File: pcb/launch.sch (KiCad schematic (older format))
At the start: 241 parts, among them J1 DNP, U1 ATmega32U4-MU, Y0 ECS-160-18-23G-JGN-TR

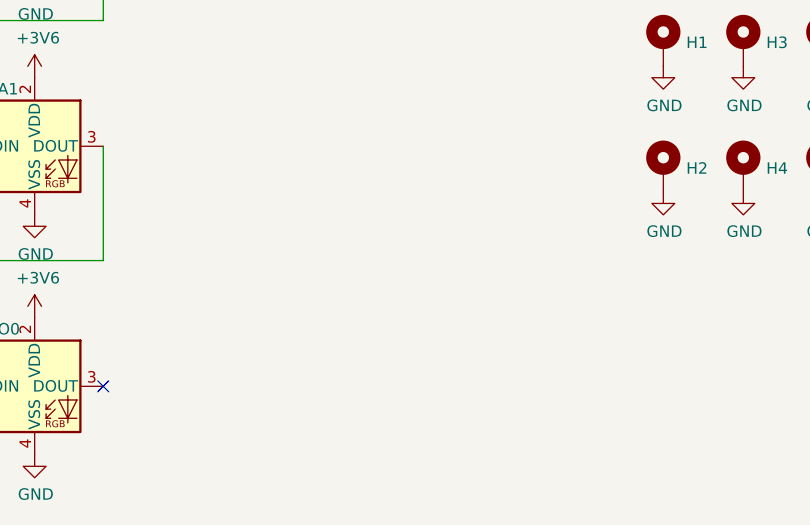
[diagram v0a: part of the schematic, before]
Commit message: add logo to schematic, link with PCB
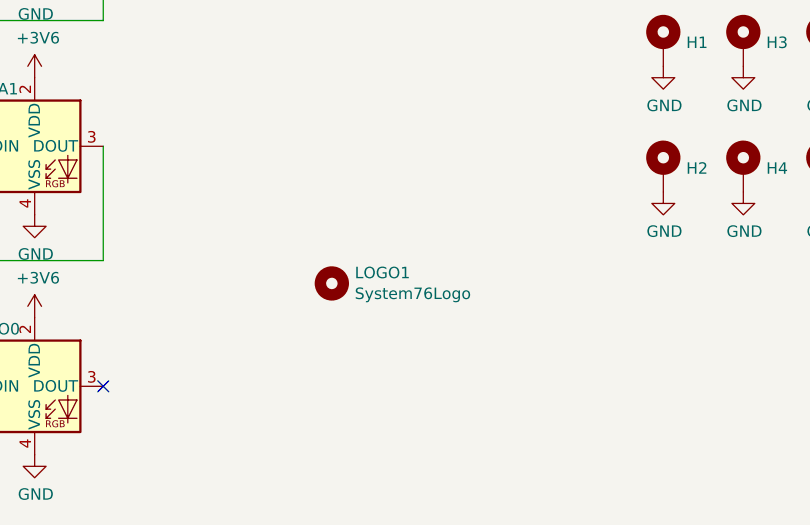
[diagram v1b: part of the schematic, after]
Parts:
- added LOGO1: System76Logo, Logo:System76, symbol Mechanical:MountingHole
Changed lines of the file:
@@
+	1    0    0    -1
+$EndComp
+$Comp
+L Mechanical:MountingHole LOGO1
+U 1 1 60A8F9E7
+P 10700 10100
+F 0 "LOGO1" H 10800 10146 50  0000 L CNN
+F 1 "System76Logo" H 10800 10055 50  0000 L CNN
+F 2 "Logo:System76" H 10700 10100 50  0001 C CNN
+F 3 "~" H 10700 10100 50  0001 C CNN
+	1    10700 10100
 	1    0    0    -1
 $EndComp

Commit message: Fix library references for symbols renamed in upstream also remove cache from gitignore, include in repo in case user's libaries don't align.
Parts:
- D10, D11, D12, D13, D14, D15, D16, D17, D18, D19, D20, D21, D22, D23, D24, D25, D26, D27, D28, D29, D30, D31, D32, D33, D34, D35, D36, D37, D38, D39, D40, D41, D42, D43, D44, D45, D46, D47, D48, D49, D50, D9: symbol Device:D_x2_KCom_AAK -> Device:D_Dual_CommonCathode_AAK
- U1: symbol MCU_Microchip_ATmega:ATmega32U4-MU -> MCU_Microchip_ATmega:ATmega32U4-M
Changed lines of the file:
@@
 LED
 $Comp
-L MCU_Microchip_ATmega:ATmega32U4-MU U1
+L MCU_Microchip_ATmega:ATmega32U4-M U1
 U 1 1 5E72DD65
 P 14600 6200
@@
 Wire Wire Line
 	14500 8000 14600 8000
-Connection ~ 14600 8000
 Text GLabel 15200 4800 2    50   Input ~ 0
 SCLK
@@
 Connection ~ 1750 2300
 $Comp
-L Device:D_x2_KCom_AAK D9
+L Device:D_Dual_CommonCathode_AAK D9
 U 1 1 6068616E
 P 1750 1500
@@
 $EndComp
 $Comp
-L Device:D_x2_KCom_AAK D10
+L Device:D_Dual_CommonCathode_AAK D10
 U 1 1 6097330F
 P 1750 2000
@@
 	2450 1500 2450 2000
 $Comp
-L Device:D_x2_KCom_AAK D11
+L Device:D_Dual_CommonCathode_AAK D11
 U 1 1 60994697
 P 1750 2500
@@
 	950  4300 1750 4300
 $Comp
-L Device:D_x2_KCom_AAK D12
+L Device:D_Dual_CommonCathode_AAK D12
 U 1 1 60A3ED72
 P 1750 3000
@@
 $EndComp
 $Comp
-L Device:D_x2_KCom_AAK D13
+L Device:D_Dual_CommonCathode_AAK D13
 U 1 1 60A3F73E
 P 1750 3500
@@
 $EndComp
 $Comp
-L Device:D_x2_KCom_AAK D14
+L Device:D_Dual_CommonCathode_AAK D14
 U 1 1 60A40011
 P 1750 4000
@@
 Connection ~ 11050 5800
 $Comp
-L Device:D_x2_KCom_AAK D15
+L Device:D_Dual_CommonCathode_AAK D15
 U 1 1 60CB7B22
 P 10750 1500
@@
 $EndComp
 $Comp
-L Device:D_x2_KCom_AAK D16
+L Device:D_Dual_CommonCathode_AAK D16
 U 1 1 60CC23F5
 P 10750 2000
@@
 $EndComp
 $Comp
-L Device:D_x2_KCom_AAK D18
+L Device:D_Dual_CommonCathode_AAK D18
 U 1 1 60CC3D8E
 P 10750 3000
@@
 $EndComp
 $Comp
-L Device:D_x2_KCom_AAK D19
+L Device:D_Dual_CommonCathode_AAK D19
 U 1 1 60CC4A93
 P 10750 3500
@@
 $EndComp
 $Comp
-L Device:D_x2_KCom_AAK D20
+L Device:D_Dual_CommonCathode_AAK D20
 U 1 1 60CC5708
 P 10750 4000
@@
 	9950 3500 9950 4000
 $Comp
-L Device:D_x2_KCom_AAK D21
+L Device:D_Dual_CommonCathode_AAK D21
 U 1 1 60EB4E93
 P 9250 1500
@@
 $EndComp
 $Comp
-L Device:D_x2_KCom_AAK D22
+L Device:D_Dual_CommonCathode_AAK D22
 U 1 1 60EB4E9D
 P 9250 2000
@@
 $EndComp
 $Comp
-L Device:D_x2_KCom_AAK D23
+L Device:D_Dual_CommonCathode_AAK D23
 U 1 1 60EB4EA7
 P 9250 2500
@@
 $EndComp
 $Comp
-L Device:D_x2_KCom_AAK D24
+L Device:D_Dual_CommonCathode_AAK D24
 U 1 1 60EB4EB1
 P 9250 3000
@@
 $EndComp
 $Comp
-L Device:D_x2_KCom_AAK D25
+L Device:D_Dual_CommonCathode_AAK D25
 U 1 1 60EB4EBB
 P 9250 3500
@@
 $EndComp
 $Comp
-L Device:D_x2_KCom_AAK D26
+L Device:D_Dual_CommonCathode_AAK D26
 U 1 1 60EB4EC5
 P 9250 4000
@@
 	8450 800  8450 1500
 $Comp
-L Device:D_x2_KCom_AAK D27
+L Device:D_Dual_CommonCathode_AAK D27
 U 1 1 610F954C
 P 7750 1500
@@
 $EndComp
 $Comp
-L Device:D_x2_KCom_AAK D28
+L Device:D_Dual_CommonCathode_AAK D28
 U 1 1 610F9556
 P 7750 2000
@@
 $EndComp
 $Comp
-L Device:D_x2_KCom_AAK D29
+L Device:D_Dual_CommonCathode_AAK D29
 U 1 1 610F9560
 P 7750 2500
@@
 $EndComp
 $Comp
-L Device:D_x2_KCom_AAK D30
+L Device:D_Dual_CommonCathode_AAK D30
 U 1 1 610F956A
 P 7750 3000
@@
 $EndComp
 $Comp
-L Device:D_x2_KCom_AAK D31
+L Device:D_Dual_CommonCathode_AAK D31
 U 1 1 610F9574
 P 7750 3500
@@
 $EndComp
 $Comp
-L Device:D_x2_KCom_AAK D32
+L Device:D_Dual_CommonCathode_AAK D32
 U 1 1 610F957E
 P 7750 4000
@@
 	7050 3500 7050 4000
 $Comp
-L Device:D_x2_KCom_AAK D33
+L Device:D_Dual_CommonCathode_AAK D33
 U 1 1 6136DAE4
 P 6250 1500
@@
 $EndComp
 $Comp
-L Device:D_x2_KCom_AAK D34
+L Device:D_Dual_CommonCathode_AAK D34
 U 1 1 6136DAEE
 P 6250 2000
@@
 $EndComp
 $Comp
-L Device:D_x2_KCom_AAK D35
+L Device:D_Dual_CommonCathode_AAK D35
 U 1 1 6136DAF8
 P 6250 2500
@@
 $EndComp
 $Comp
-L Device:D_x2_KCom_AAK D36
+L Device:D_Dual_CommonCathode_AAK D36
 U 1 1 6136DB02
 P 6250 3000
@@
 $EndComp
 $Comp
-L Device:D_x2_KCom_AAK D37
+L Device:D_Dual_CommonCathode_AAK D37
 U 1 1 6136DB0C
 P 6250 3500
@@
 $EndComp
 $Comp
-L Device:D_x2_KCom_AAK D38
+L Device:D_Dual_CommonCathode_AAK D38
 U 1 1 6136DB16
 P 6250 4000
@@
 	5550 3500 5550 4000
 $Comp
-L Device:D_x2_KCom_AAK D39
+L Device:D_Dual_CommonCathode_AAK D39
 U 1 1 61589051
 P 4750 1500
@@
 $EndComp
 $Comp
-L Device:D_x2_KCom_AAK D40
+L Device:D_Dual_CommonCathode_AAK D40
 U 1 1 6158905B
 P 4750 2000
@@
 $EndComp
 $Comp
-L Device:D_x2_KCom_AAK D41
+L Device:D_Dual_CommonCathode_AAK D41
 U 1 1 61589065
 P 4750 2500
@@
 $EndComp
 $Comp
-L Device:D_x2_KCom_AAK D42
+L Device:D_Dual_CommonCathode_AAK D42
 U 1 1 6158906F
 P 4750 3000
@@
 $EndComp
 $Comp
-L Device:D_x2_KCom_AAK D43
+L Device:D_Dual_CommonCathode_AAK D43
 U 1 1 61589079
 P 4750 3500
@@
 $EndComp
 $Comp
-L Device:D_x2_KCom_AAK D44
+L Device:D_Dual_CommonCathode_AAK D44
 U 1 1 61589083
 P 4750 4000
@@
 	4050 3500 4050 4000
 $Comp
-L Device:D_x2_KCom_AAK D45
+L Device:D_Dual_CommonCathode_AAK D45
 U 1 1 617A8B21
 P 3250 1500
@@
 $EndComp
 $Comp
-L Device:D_x2_KCom_AAK D46
+L Device:D_Dual_CommonCathode_AAK D46
 U 1 1 617A8B2B
 P 3250 2000
@@
 $EndComp
 $Comp
-L Device:D_x2_KCom_AAK D47
+L Device:D_Dual_CommonCathode_AAK D47
 U 1 1 617A8B35
 P 3250 2500
@@
 $EndComp
 $Comp
-L Device:D_x2_KCom_AAK D48
+L Device:D_Dual_CommonCathode_AAK D48
 U 1 1 617A8B3F
 P 3250 3000
@@
 $EndComp
 $Comp
-L Device:D_x2_KCom_AAK D49
+L Device:D_Dual_CommonCathode_AAK D49
 U 1 1 617A8B49
 P 3250 3500
@@
 $EndComp
 $Comp
-L Device:D_x2_KCom_AAK D50
+L Device:D_Dual_CommonCathode_AAK D50
 U 1 1 617A8B53
 P 3250 4000
@@
 	3250 3800 4750 3800
 $Comp
-L Device:D_x2_KCom_AAK D17
+L Device:D_Dual_CommonCathode_AAK D17
 U 1 1 60CC31D9
 P 10750 2500
